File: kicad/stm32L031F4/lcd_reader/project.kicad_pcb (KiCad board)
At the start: 2 copper layers, 24 x 43 mm, 22 parts, among them J1 WAKE, J13 GND_EXT, J2 SWD, J8 RADIO, Q1 CSD16414Q5, U1 74LS14, U2 STM32L031F4Px, U3 74LS14

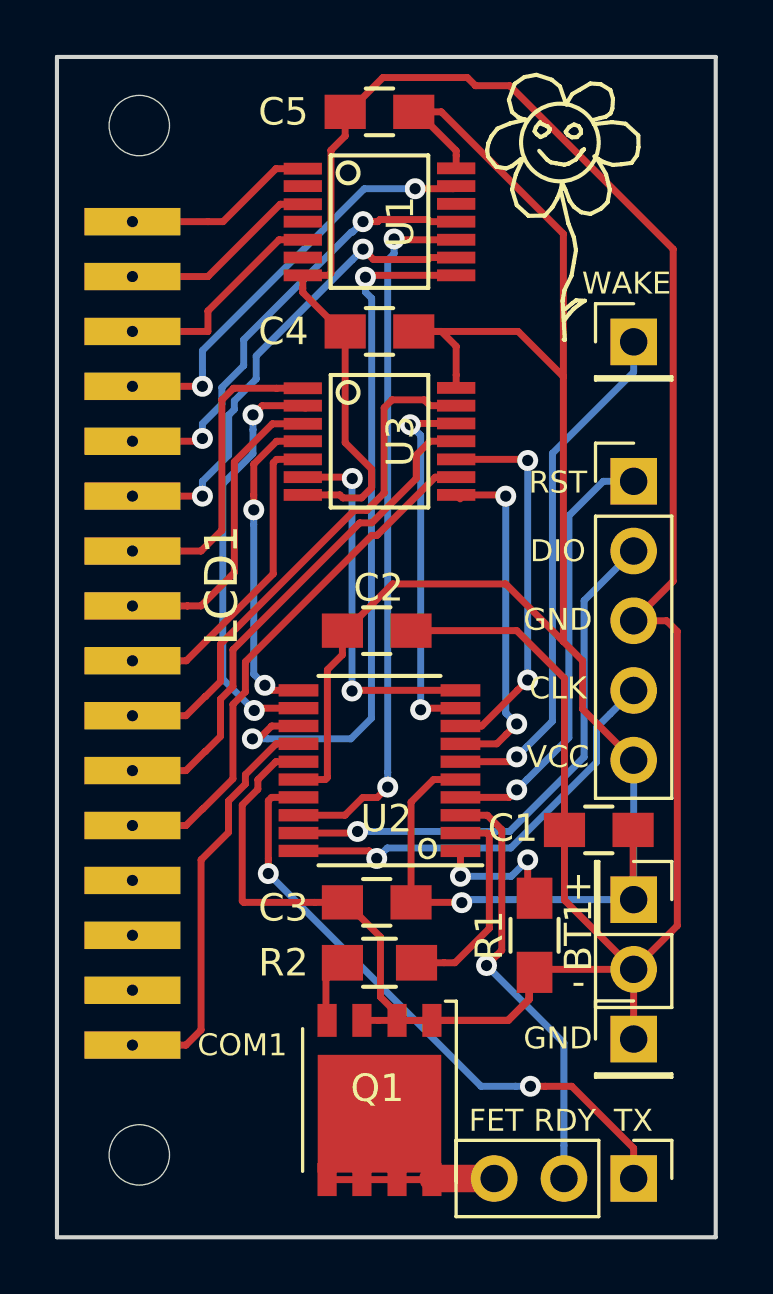
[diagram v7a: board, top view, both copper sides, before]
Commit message: SOIC-14 for the schmitt triggers
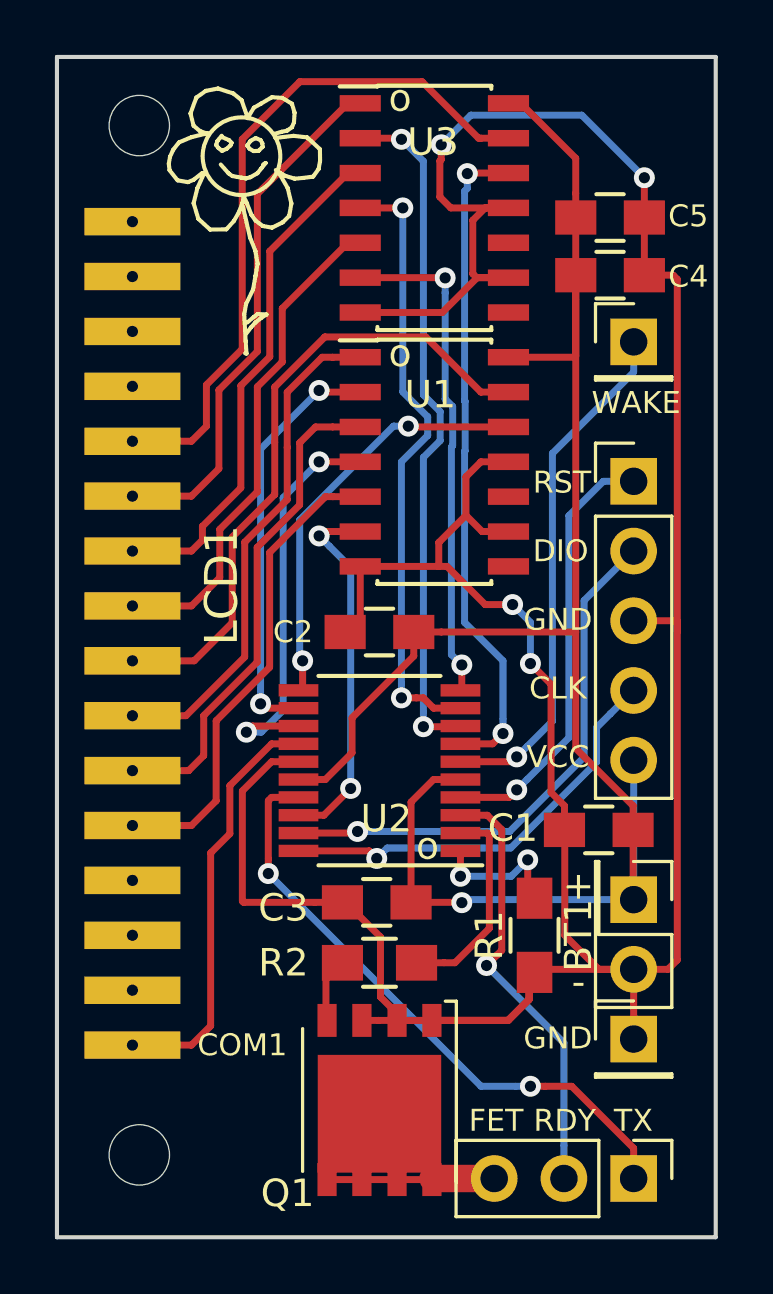
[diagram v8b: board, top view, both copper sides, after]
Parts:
- U1, U3: footprint SMD_Packages:SSOP-14 -> Housings_SOIC:SOIC-14_3.9x8.7mm_Pitch1.27mm
- moved REF** 39.7 mm to (237.1, 93.4)
- moved REF** 11.6 mm to (223.4, 94.2)
- moved C5 9.24 mm to (236.2, 99.3), turned to 180 degrees
- moved U1 8.98 mm to (229.8, 108.2), turned to 0 degrees
- moved U3 8.73 mm to (229.8, 99.0), turned to 0 degrees
- moved C4 8.65 mm to (236.2, 101.5), turned to 180 degrees
- moved C2 0.11 mm to (227.8, 114.5), turned to 180 degrees
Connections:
- LCD1 pad 13: /COM4 -> /COM2
- LCD1 pad 15: /COM2 -> /COM4
- U1 pad 1: Net-(LCD1-Pad1) -> Net-(LCD1-Pad10)
- U1 pad 10: IN8 -> Net-(U1-Pad10)
- U1 pad 11: Net-(LCD1-Pad5) -> GND
- U1 pad 12: Net-(U1-Pad12) -> IN5
- U1 pad 13: Net-(LCD1-Pad4) -> Net-(LCD1-Pad9)
- U1 pad 2: Net-(U1-Pad2) -> IN6
- U1 pad 3: Net-(LCD1-Pad2) -> Net-(LCD1-Pad11)
- U1 pad 4: Net-(U1-Pad4) -> IN7
- U1 pad 5: Net-(LCD1-Pad3) -> Net-(LCD1-Pad12)
- U1 pad 6: Net-(U1-Pad6) -> IN8
- U1 pad 8: IN7 -> Net-(U1-Pad8)
- U1 pad 9: Net-(LCD1-Pad6) -> GND
- U3 pad 1: Net-(LCD1-Pad7) -> Net-(LCD1-Pad6)
- U3 pad 10: IN2 -> Net-(U3-Pad10)
- U3 pad 11: Net-(LCD1-Pad11) -> GND
- U3 pad 12: IN3 -> IN1
- U3 pad 13: Net-(LCD1-Pad10) -> Net-(LCD1-Pad5)
- U3 pad 2: IN6 -> IN2
- U3 pad 3: Net-(LCD1-Pad8) -> Net-(LCD1-Pad7)
- U3 pad 4: IN5 -> IN3
- U3 pad 5: Net-(LCD1-Pad9) -> Net-(LCD1-Pad8)
- U3 pad 8: IN1 -> Net-(U3-Pad8)
- U3 pad 9: Net-(LCD1-Pad12) -> GND
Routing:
- net Net-(LCD1-Pad4): track 15.6 -> 0.00 mm, vias 2 -> 0
- net IN8: track 26.1 -> 13.5 mm
- net Net-(LCD1-Pad9): track 11.6 -> 23.5 mm
- net IN1: track 12.8 -> 24.3 mm
- net IN2: track 13.8 -> 25.1 mm
- net IN7: track 26.0 -> 14.8 mm
- net Net-(LCD1-Pad5): track 16.4 -> 25.3 mm, vias 2 -> 0
- net IN3: track 13.7 -> 22.5 mm
- net +BATT: track 77.6 -> 69.2 mm
- net GND: track 119.1 -> 127.3 mm, vias 0 -> 4
- net Net-(LCD1-Pad3): track 8.03 -> 0.00 mm
- net Net-(LCD1-Pad2): track 7.30 -> 0.00 mm
- net Net-(LCD1-Pad7): track 11.4 -> 18.7 mm
- net Net-(LCD1-Pad1): track 7.01 -> 0.00 mm
- net Net-(LCD1-Pad8): track 11.3 -> 18.2 mm
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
